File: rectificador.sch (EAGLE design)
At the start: 26 parts, among them T1 TYN612, X2 X2

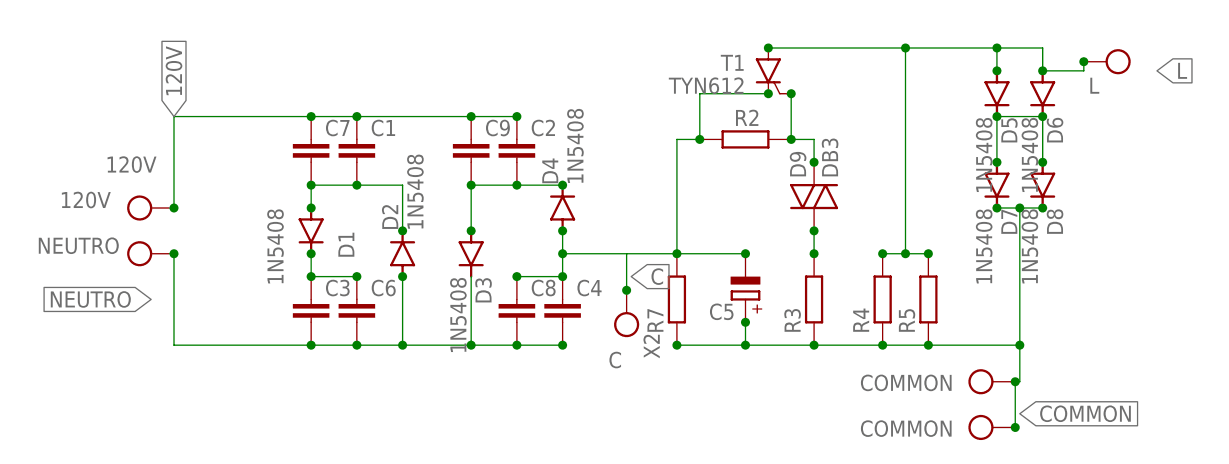
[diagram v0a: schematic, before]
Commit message: feat: add 3D packages.
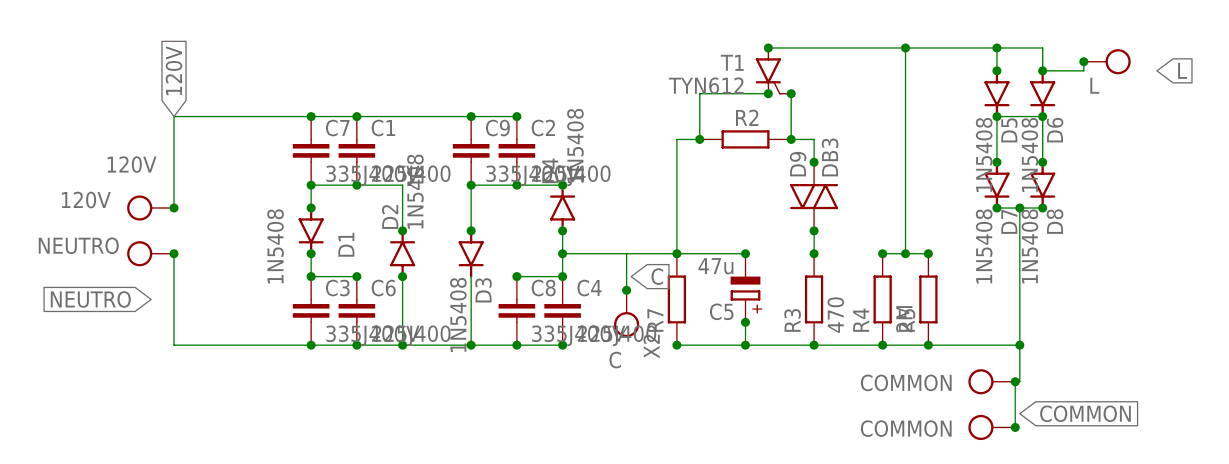
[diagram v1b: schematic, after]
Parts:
- C1, C2, C4: value (none) -> 225J400
- C3, C7, C8, C9: value (none) -> 335J400V
- C5: value (none) -> 47u
- C6: value (none) -> 225J400; SPICEPREFIX (none) -> C
- R3: value (none) -> 470
- R4: value (none) -> 2M
